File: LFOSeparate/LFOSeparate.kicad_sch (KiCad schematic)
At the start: 31 parts, among them IC1 PIC16F15325-I_P, IC2 MCP6232-E_P, IC3 MCP6232-E_P, J1 ICSP, J2 D_Power, J3 Input, J4 Output, J5 A_Power, U1 Opamp_Dual

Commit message: LFOSeparate
アートワーク作成中
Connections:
- net +5VD: now also J1.4 (Pin_4); no longer J1.2 (Pin_2)
- net GNDA: now also J4.11 (Pin_11); no longer J4.6 (Pin_6)
- net ICSPCLK: now also J1.1 (Pin_1); no longer J1.5 (Pin_5)
- net ICSPDT: now also J1.2 (Pin_2); no longer J1.4 (Pin_4)
- net Randum: now also J4.7 (Pin_7), J4.8 (Pin_8); no longer J4.10 (Pin_10), J4.4 (Pin_4)
- net Sine: now also J4.2 (Pin_2); no longer J4.7 (Pin_7)
- net Square: now also J4.5 (Pin_5), J4.6 (Pin_6); no longer J4.3 (Pin_3), J4.9 (Pin_9)
- net Triangle: now also J4.3 (Pin_3), J4.4 (Pin_4); no longer J4.2 (Pin_2), J4.8 (Pin_8)
- net ~MCLR: now also J1.5 (Pin_5); no longer J1.1 (Pin_1)
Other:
- moved on the sheet: J1

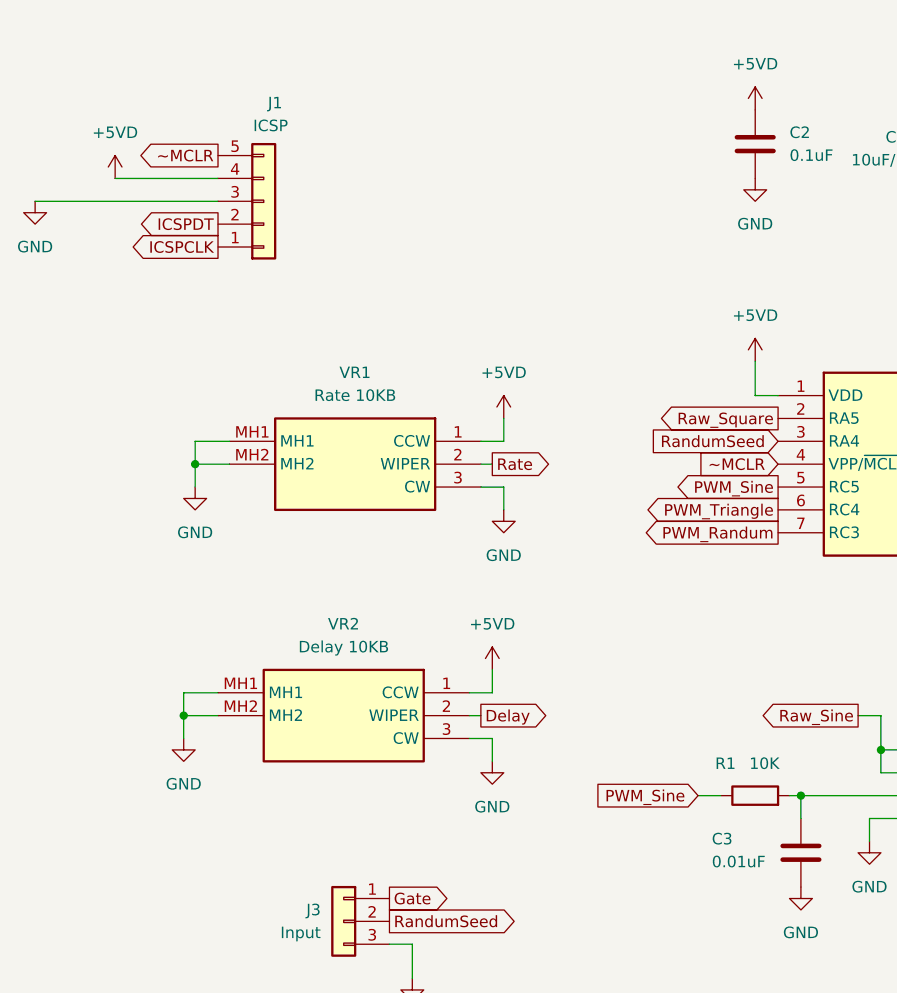
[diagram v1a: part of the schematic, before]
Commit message: LFOSeparate
LFOSeparateは配線完了
EGSeparateは回路図作成中
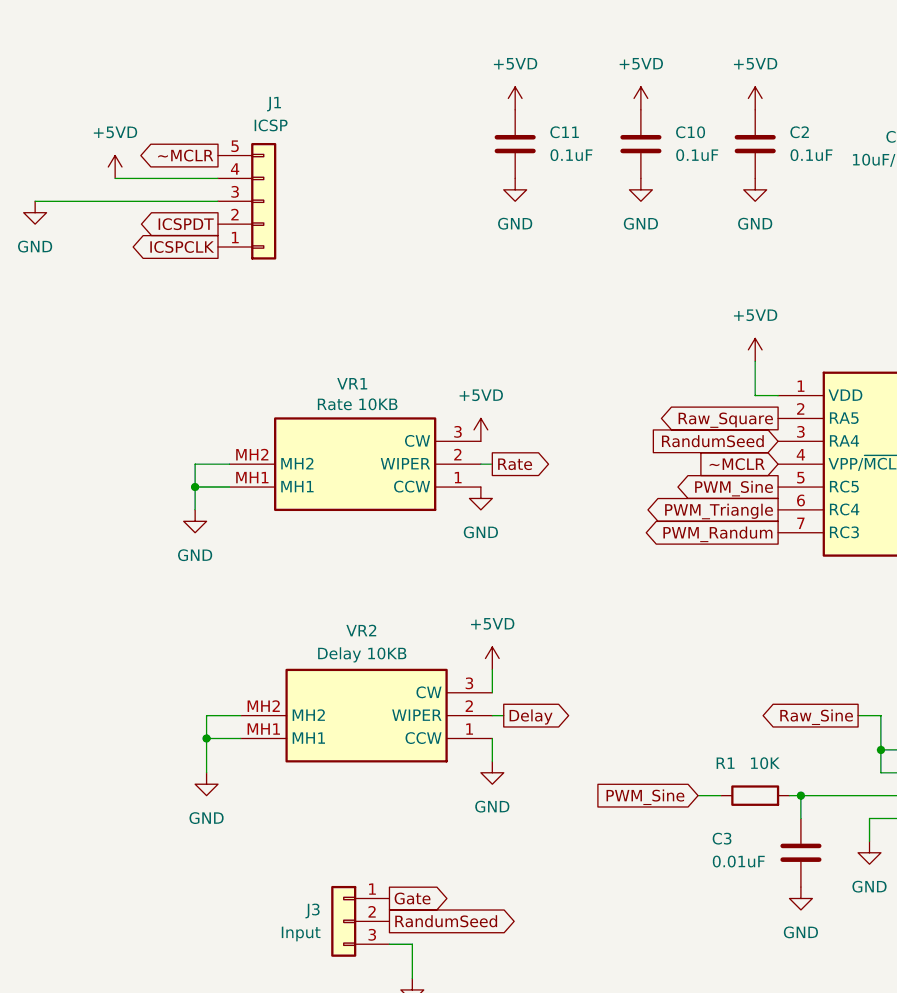
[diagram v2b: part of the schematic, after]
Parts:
- added C10, C11: 0.1uF, Capacitor_SMD:C_0805_2012Metric_Pad1.18x1.45mm_HandSolder, symbol Device:C
- C2, C6, C7: footprint Capacitor_THT:C_Disc_D5.0mm_W2.5mm_P2.50mm -> Capacitor_SMD:C_0805_2012Metric_Pad1.18x1.45mm_HandSolder
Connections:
- net +5VD: now also VR1.3 (CW), VR2.3 (CW), C10.1, C11.1; no longer VR1.1 (CCW), VR2.1 (CCW)
- net GND: now also VR1.1 (CCW), VR2.1 (CCW), C10.2, C11.2; no longer VR1.3 (CW), VR2.3 (CW)
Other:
- moved on the sheet: VR1, VR2

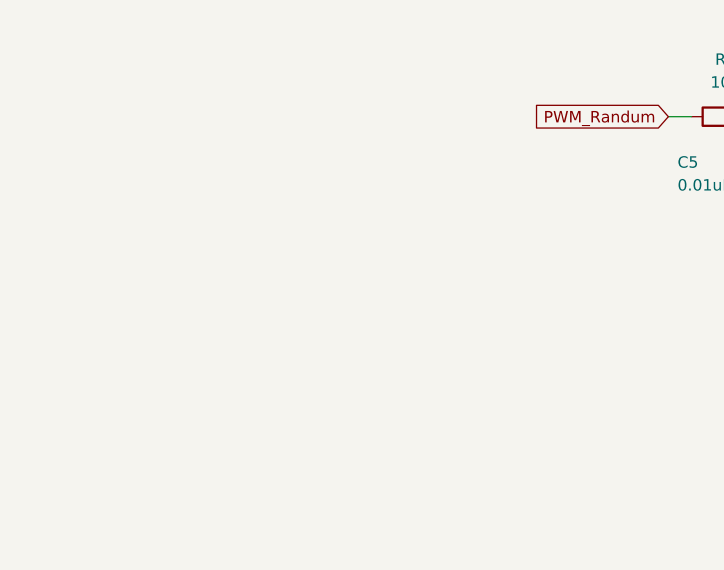
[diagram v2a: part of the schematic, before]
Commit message: MC2
アクセントレベルを追加したEGACCを登録
回路全般部品配置済
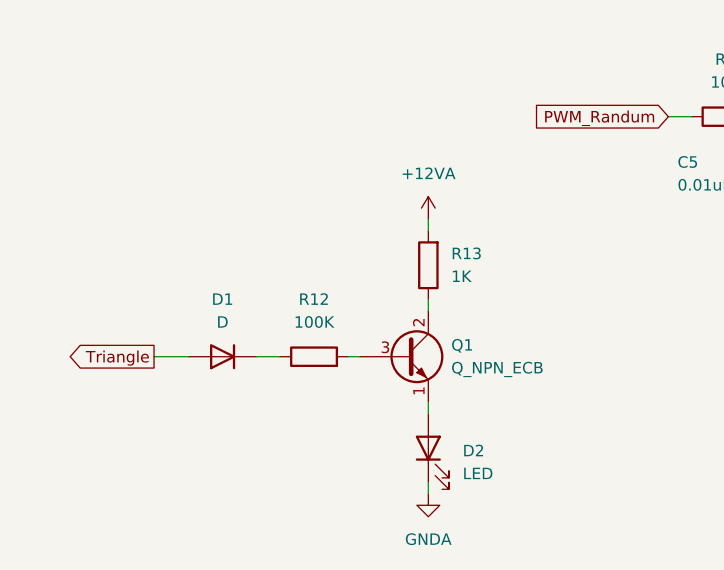
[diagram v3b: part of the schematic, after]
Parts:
- added D1: D, Diode_THT:D_DO-34_SOD68_P2.54mm_Vertical_AnodeUp, symbol Device:D
- added D2: LED, LED_THT:LED_D5.0mm_FlatTop, symbol Device:LED
- added Q1: Q_NPN_ECB, Package_TO_SOT_THT:TO-92_HandSolder, symbol Device:Q_NPN_ECB
- added R12: 100K, Resistor_THT:R_Axial_DIN0204_L3.6mm_D1.6mm_P2.54mm_Vertical, symbol Device:R
- added R13: 1K, Resistor_THT:R_Axial_DIN0204_L3.6mm_D1.6mm_P2.54mm_Vertical, symbol Device:R
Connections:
- net +12VA: now also R13.2
- net GNDA: now also D2.1 (K)
- net Triangle: now also D1.2 (A)
- new net: D2.2 (A), Q1.1 (E)
- new net: Q1.2 (C), R13.1
- new net: Q1.3 (B), R12.2
- new net: D1.1 (K), R12.1

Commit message: LFOSeparate
プログラムと回路のデバッグ後の修正を反映
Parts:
- removed D1: D, Diode_THT:D_DO-34_SOD68_P2.54mm_Vertical_AnodeUp, symbol Device:D
- added C12: 0.01uF, Capacitor_THT:C_Disc_D3.4mm_W2.1mm_P2.50mm, symbol Device:C
- added R14: 1K, Resistor_THT:R_Axial_DIN0204_L3.6mm_D1.6mm_P2.54mm_Vertical, symbol Device:R
- added R15: 100, Resistor_THT:R_Axial_DIN0204_L3.6mm_D1.6mm_P2.54mm_Vertical, symbol Device:R
- C8, C9: value 1uF/16V -> 47uF/16V
- R11: value 12K -> 1.2K
- R13: value 1K -> 2.2K
- R5: value 10K -> 30K
- R6: value 3.9K -> 20K
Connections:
- net +12VA: now also D2.2 (A); no longer R13.2
- net +5VD: now also R14.2
- net GND: now also IC3.5 (VINB+), C12.2
- net GNDA: now also Q1.1 (E), R10.1, R6.2; no longer D2.1 (K), U1.3 (+), U1.6 (-)
- net Raw_Sine: now also R5.1; no longer C8.1
- net Square: now also IC1.11 (RA2); no longer IC3.6 (VINB-), IC3.7 (VOUTB)
- net Triangle: now also R12.1
- net ~MCLR: now also R15.2
- net at R7.1, U1.1: now also U1.2 (-); no longer R6.2
- net at C8.2, R4.2: now also U1.3 (+); no longer R5.1
- net at R5.2, R6.1: now also C8.1; no longer U1.2 (-)
- net at R10.2, R11.1: now also U1.6 (-); no longer U1.5 (+)
- net at C9.2, R9.2: now also U1.5 (+); no longer R10.1
- net Raw_Square: no longer names the net of IC1.2 (RA5)
- net Raw_Square: no longer IC3.5 (VINB+)
- new net: C12.1, R14.1, R15.1
- new net: IC3.6 (VINB-), IC3.7 (VOUTB)
- new net: D2.1 (K), R13.2
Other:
- moved on the sheet: C8, C9, D2, J1, J4, R10, R11, R4, R5, R6, R7, R8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
